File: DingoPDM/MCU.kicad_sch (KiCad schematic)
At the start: 23 parts, among them J4 TC, U3 PCA82C250, U4 STM32F303CCTx, Y1 8mHz

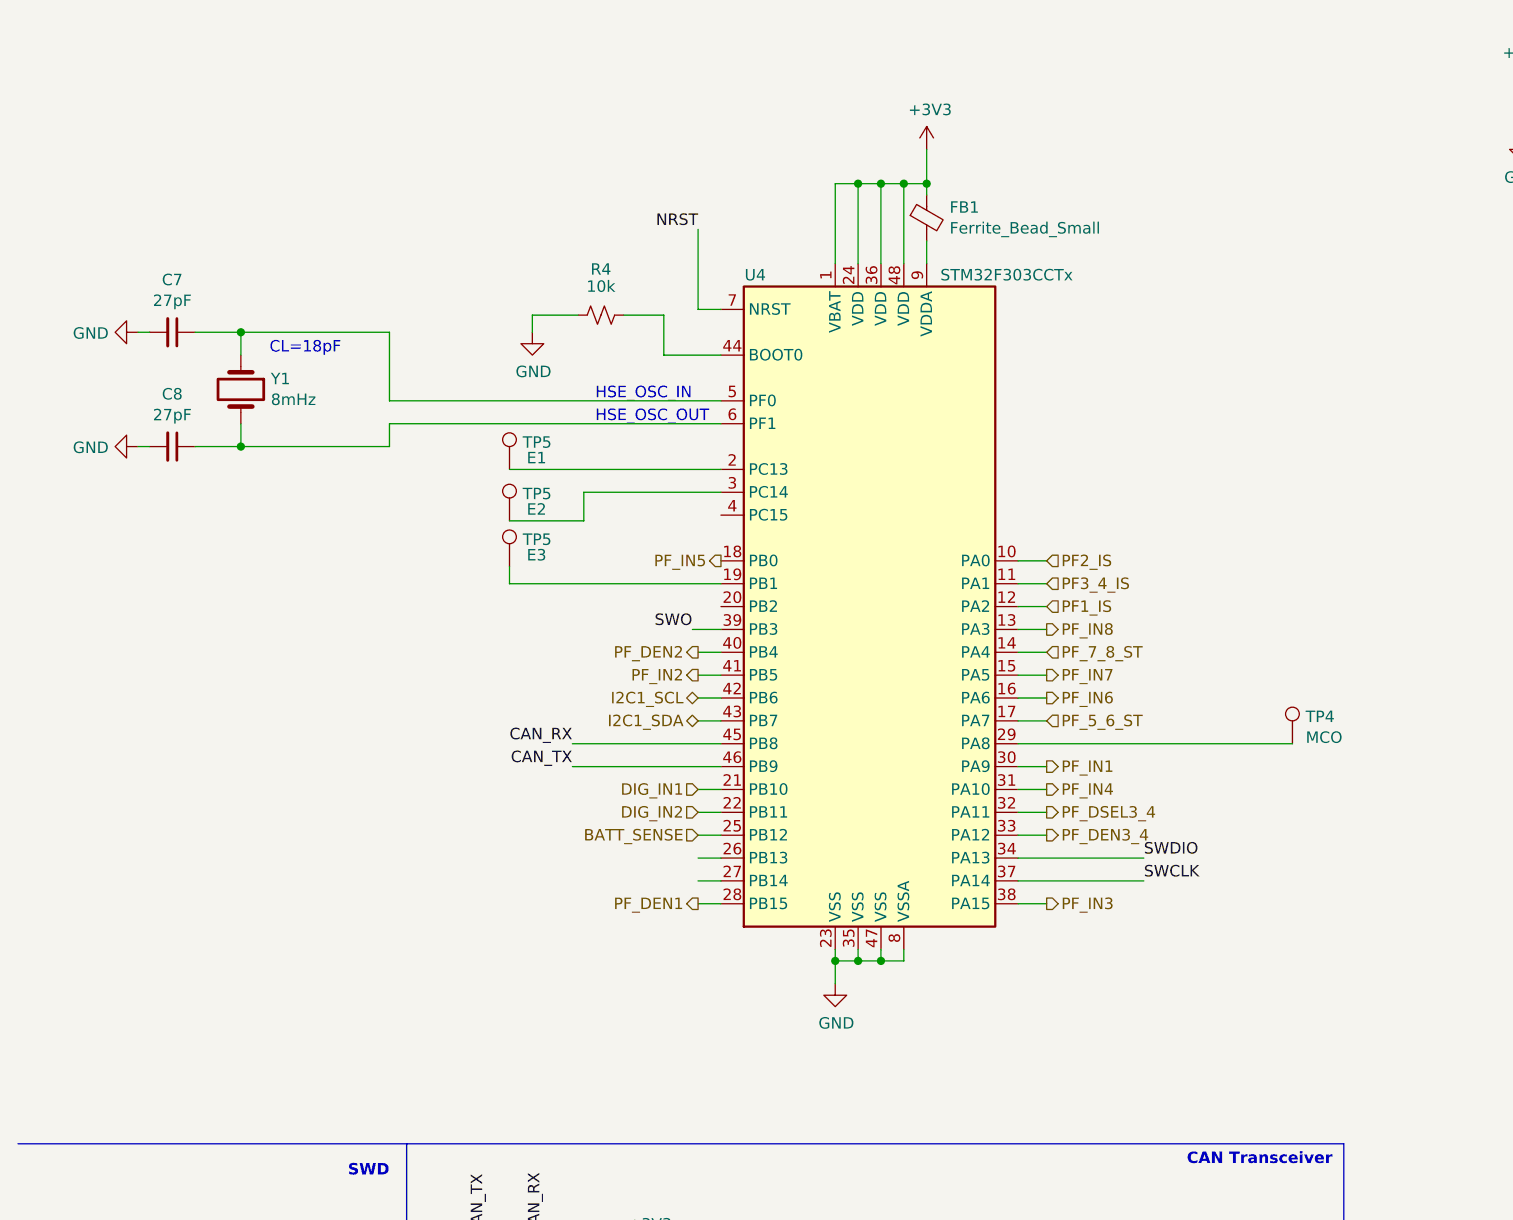
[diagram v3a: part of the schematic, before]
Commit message: Changed to STM32F446RE
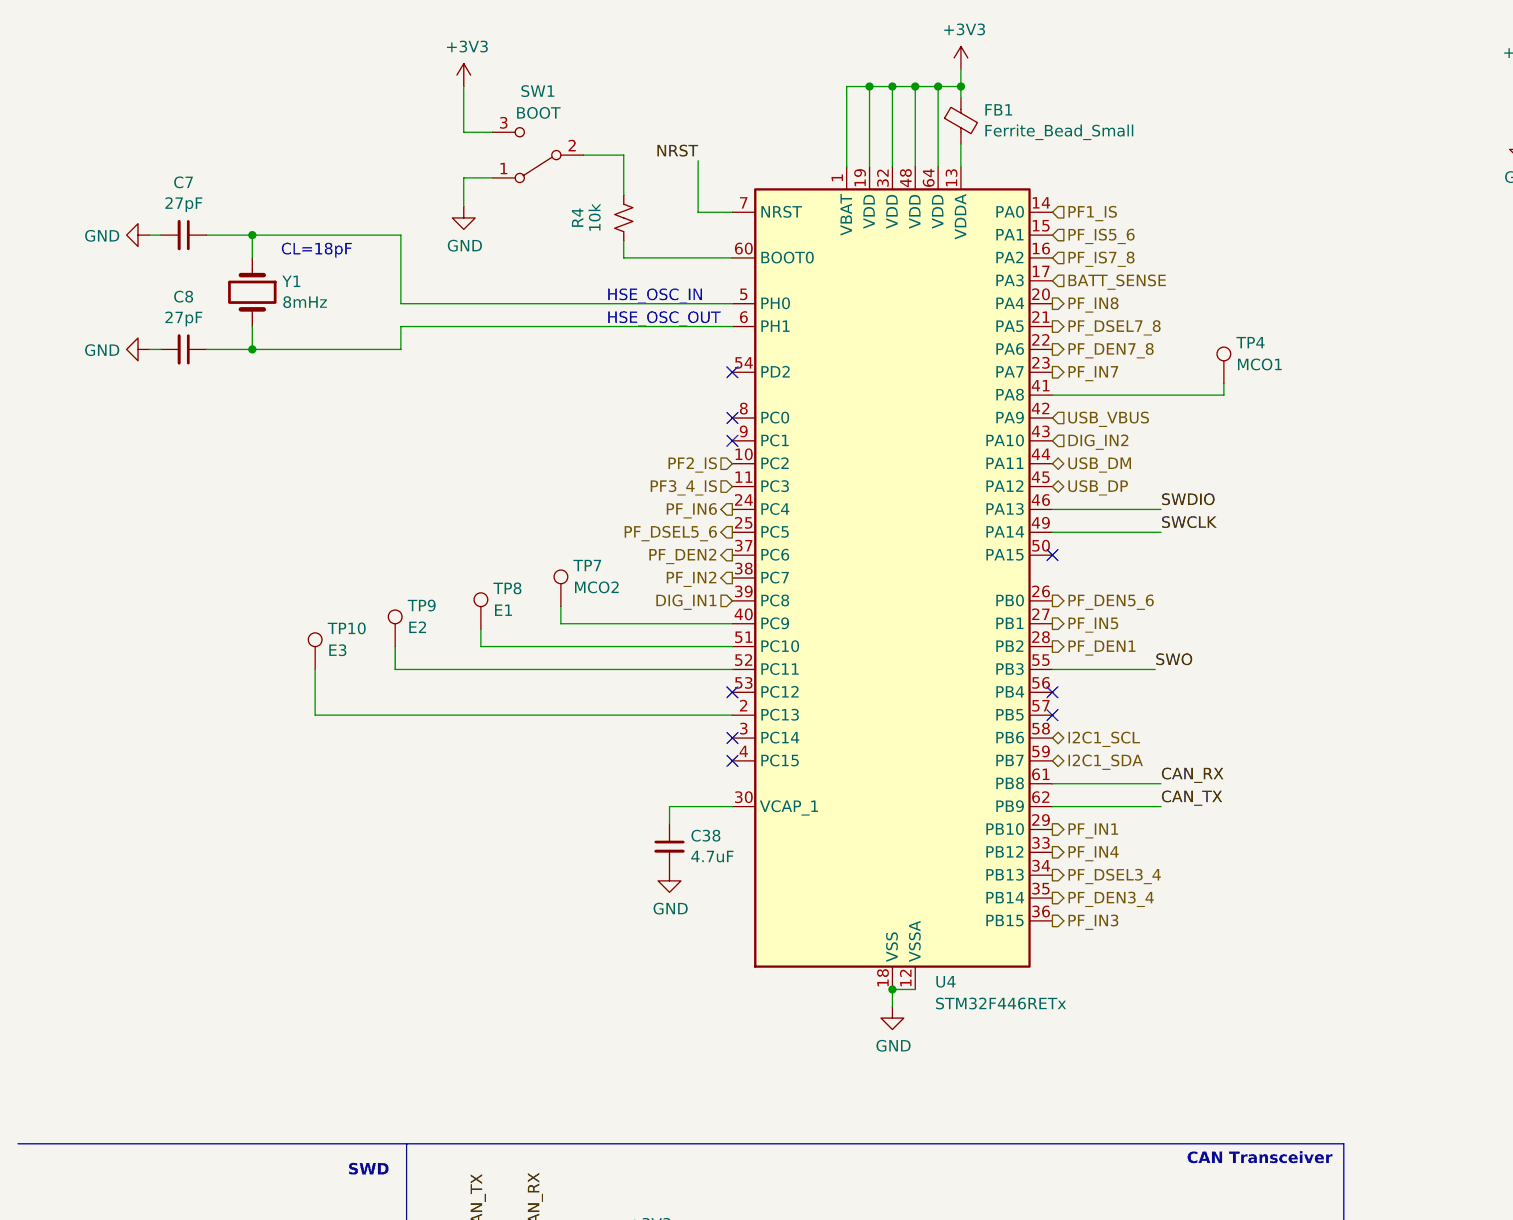
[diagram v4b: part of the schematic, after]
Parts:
- removed TP5: E1, TestPoint:TestPoint_Keystone_5000-5004_Miniature, symbol Connector:TestPoint
- removed TP5: E2, TestPoint:TestPoint_Keystone_5000-5004_Miniature, symbol Connector:TestPoint
- removed TP5: E3, TestPoint:TestPoint_Keystone_5000-5004_Miniature, symbol Connector:TestPoint
- removed U4: STM32F303CCTx, Package_QFP:LQFP-48_7x7mm_P0.5mm, symbol MCU_ST_STM32F3:STM32F303CCTx
- added C38: 4.7uF, Capacitor_SMD:C_0805_2012Metric, symbol Device:C_Small
- added SW1: BOOT, SlideSwitch:CJS-1200TB, symbol Switch:SW_SPDT
- added TP10: E3, TestPoint:TestPoint_Keystone_5000-5004_Miniature, symbol Connector:TestPoint
- added TP7: MCO2, TestPoint:TestPoint_Pad_D1.0mm, symbol Connector:TestPoint
- added TP8: E1, TestPoint:TestPoint_Keystone_5000-5004_Miniature, symbol Connector:TestPoint
- added TP9: E2, TestPoint:TestPoint_Keystone_5000-5004_Miniature, symbol Connector:TestPoint
- added U4: STM32F446RETx, Package_QFP:LQFP-64_10x10mm_P0.5mm, symbol MCU_ST_STM32F4:STM32F446RETx
- TP4: value MCO -> MCO1
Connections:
- net +3V3: now also SW1.3 (C), U4.1 (VBAT), U4.19 (VDD), U4.32 (VDD), U4.48 (VDD), U4.64 (VDD)
- net BATT_SENSE: now also U4.17 (PA3)
- net CAN_RX: now also U4.61 (PB8)
- net CAN_TX: now also U4.62 (PB9)
- net DIG_IN1: now also U4.39 (PC8)
- net DIG_IN2: now also U4.43 (PA10)
- net GND: now also C38.2, SW1.1 (A), U4.12 (VSSA), U4.18 (VSS), U4.31 (VSS), U4.47 (VSS), U4.63 (VSS); no longer R4.2
- net I2C1_SCL: now also U4.58 (PB6)
- net I2C1_SDA: now also U4.59 (PB7)
- net NRST: now also U4.7 (NRST)
- net PF1_IS: now also U4.14 (PA0)
- net PF2_IS: now also U4.10 (PC2)
- net PF3_4_IS: now also U4.11 (PC3)
- net PF_DEN1: now also U4.28 (PB2)
- net PF_DEN2: now also U4.37 (PC6)
- net PF_DEN3_4: now also U4.35 (PB14)
- net PF_DSEL3_4: now also U4.34 (PB13)
- net PF_IN1: now also U4.29 (PB10)
- net PF_IN2: now also U4.38 (PC7)
- net PF_IN3: now also U4.36 (PB15)
- net PF_IN4: now also U4.33 (PB12)
- net PF_IN5: now also U4.27 (PB1)
- net PF_IN6: now also U4.24 (PC4)
- net PF_IN7: now also U4.23 (PA7)
- net PF_IN8: now also U4.20 (PA4)
- net SWCLK: now also U4.49 (PA14)
- net SWDIO: now also U4.46 (PA13)
- net SWO: now also U4.55 (PB3)
- net at TP4.1: now also U4.41 (PA8)
- net at R4.1: now also SW1.2 (B)
- net at C7.1, Y1.1: now also U4.5 (PH0)
- net at C8.1, Y1.2: now also U4.6 (PH1)
- net at FB1.2: now also U4.13 (VDDA)
- new net: R4.2, U4.60 (BOOT0)
- new net: TP7.1, U4.40 (PC9)
- new net: TP8.1, U4.51 (PC10)
- new net: TP10.1, U4.2 (PC13)
- new net: TP9.1, U4.52 (PC11)
- new net: C38.1, U4.30 (VCAP_1)
- new net PF_DEN5_6: U4.26 (PB0)
- new net PF_DEN7_8: U4.22 (PA6)
- new net PF_DSEL5_6: U4.25 (PC5)
- new net PF_DSEL7_8: U4.21 (PA5)
- new net PF_IS5_6: U4.15 (PA1)
- new net PF_IS7_8: U4.16 (PA2)
- new net USB_DM: U4.44 (PA11)
- new net USB_DP: U4.45 (PA12)
- new net USB_VBUS: U4.42 (PA9)
- no-connect marks 0 -> 9
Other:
- moved on the sheet: C7, C8, FB1, R4, Y1

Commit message: Routed V7
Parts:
- removed TP4: MCO1, TestPoint:TestPoint_Pad_D1.0mm, symbol Connector:TestPoint
- removed TP7: MCO2, TestPoint:TestPoint_Pad_D1.0mm, symbol Connector:TestPoint
- added C39: 100nF, Capacitor_SMD:C_0805_2012Metric, symbol Device:C_Small
- C15: value 10nF -> 100nF; Digi-Key_PN 311-1136-1-ND -> 478-1395-1-ND; LCSC C1710 -> C49678
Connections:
- net +3V3: now also C39.1
- net DIG_IN1: now also U4.43 (PA10); no longer U4.39 (PC8)
- net DIG_IN2: now also U4.39 (PC8); no longer U4.43 (PA10)
- net GND: now also C39.2
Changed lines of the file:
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@@
   (junction (at 190.5 29.21) (diameter 0) (color 0 0 0 0)
   )
-  (junction (at 233.68 29.21) (diameter 0) (color 0 0 0 0)
-  )
   (junction (at 81.915 165.1) (diameter 0) (color 0 0 0 0)
   )
@@
   (junction (at 213.36 24.13) (diameter 0) (color 0 0 0 0)
   )
+  (junction (at 234.315 29.21) (diameter 0) (color 0 0 0 0)
+  )
+  (junction (at 234.315 24.13) (diameter 0) (color 0 0 0 0)
+  )
   (junction (at 201.93 29.21) (diameter 0) (color 0 0 0 0)
   )
@@
   (junction (at 111.76 23.495) (diameter 0) (color 0 0 0 0)
   )
-  (junction (at 233.68 24.13) (diameter 0) (color 0 0 0 0)
+  (junction (at 179.07 29.21) (diameter 0) (color 0 0 0 0)
+  )
+  (junction (at 179.07 24.13) (diameter 0) (color 0 0 0 0)
   )
   (junction (at 106.68 23.495) (diameter 0) (color 0 0 0 0)
@@
     (stroke (width 0) (type default))
   )
+  (wire (pts (xy 234.315 24.13) (xy 245.11 24.13))
+    (stroke (width 0) (type default))
+  )
+  (wire (pts (xy 234.315 29.21) (xy 245.11 29.21))
+    (stroke (width 0) (type default))
+  )
   (wire (pts (xy 111.125 167.64) (xy 130.175 167.64))
     (stroke (width 0) (type default))
@@
     (stroke (width 0) (type default))
   )
-  (wire (pts (xy 223.52 24.13) (xy 233.68 24.13))
-    (stroke (width 0) (type default))
-  )
   (wire (pts (xy 64.77 33.655) (xy 61.595 33.655))
     (stroke (width 0) (type default))
@@
     (stroke (width 0) (type default))
   )
-  (wire (pts (xy 233.68 29.21) (xy 245.11 29.21))
-    (stroke (width 0) (type default))
-  )
   (wire (pts (xy 54.61 50.165) (xy 54.61 52.705))
     (stroke (width 0) (type default))
@@
     (stroke (width 0) (type default))
   )
-  (wire (pts (xy 91.44 83.185) (xy 72.39 83.185))
-    (stroke (width 0) (type default))
-  )
   (wire (pts (xy 85.725 175.26) (xy 83.185 175.26))
     (stroke (width 0) (type default))
@@
     (stroke (width 0) (type default))
   )
-  (wire (pts (xy 127 57.785) (xy 146.05 57.785))
-    (stroke (width 0) (type default))
-  )
   (wire (pts (xy 79.375 165.1) (xy 81.915 165.1))
     (stroke (width 0) (type default))
@@
     (stroke (width 0) (type default))
   )
-  (wire (pts (xy 72.39 83.185) (xy 72.39 81.28))
-    (stroke (width 0) (type default))
-  )
   (wire (pts (xy 38.1 40.005) (xy 33.02 40.005))
     (stroke (width 0) (type default))
@@
     (stroke (width 0) (type default))
   )
-  (wire (pts (xy 233.68 24.13) (xy 245.11 24.13))
+  (wire (pts (xy 223.52 24.13) (xy 234.315 24.13))
     (stroke (width 0) (type default))
   )
@@
     (stroke (width 0) (type default))
   )
-  (wire (pts (xy 146.05 57.785) (xy 146.05 56.515))
-    (stroke (width 0) (type default))
-  )
   (wire (pts (xy 26.67 52.705) (xy 27.94 52.705))
     (stroke (width 0) (type default))
@@
     (stroke (width 0) (type default))
   )
-  (wire (pts (xy 223.52 29.21) (xy 233.68 29.21))
+  (wire (pts (xy 223.52 29.21) (xy 234.315 29.21))
     (stroke (width 0) (type default))
   )
@@
     (effects (font (size 1.27 1.27)) (justify right))
   )
-  (hierarchical_label "DIG_IN1" (shape input) (at 91.44 80.645 180) (fields_autoplaced)
+  (hierarchical_label "DIG_IN1" (shape input) (at 127 62.865 0) (fields_autoplaced)
+    (effects (font (size 1.27 1.27)) (justify left))
+  )
+  (hierarchical_label "CAN_L" (shape bidirectional) (at 140.335 172.72 0) (fields_autoplaced)
+    (effects (font (size 1.27 1.27)) (justify left))
+  )
+  (hierarchical_label "DIG_IN2" (shape input) (at 91.44 80.645 180) (fields_autoplaced)
     (effects (font (size 1.27 1.27)) (justify right))
-  )
-  (hierarchical_label "CAN_L" (shape bidirectional) (at 140.335 172.72 0) (fields_autoplaced)
-    (effects (font (size 1.27 1.27)) (justify left))
-  )
-  (hierarchical_label "DIG_IN2" (shape input) (at 127 62.865 0) (fields_autoplaced)
-    (effects (font (size 1.27 1.27)) (justify left))
   )
   (hierarchical_label "PF_DSEL3_4" (shape output) (at 127 111.125 0) (fields_autoplaced)
@@
         (path "/8948e307-9174-4227-9c28-3ff885e6e83d/00000000-0000-0000-0000-00005f4db108"
           (reference "C14") (unit 1)
-        )
-      )
-    )
-  )
-  (symbol (lib_id "Device:C_Small") (at 233.68 26.67 0) (unit 1)
-    (in_bom yes) (on_board yes) (dnp no)
-    (property "Reference" "C15" (at 236.0168 25.5016 0)
-      (effects (font (size 1.27 1.27)) (justify left))
-    )
-    (property "Value" "10nF" (at 236.0168 27.813 0)
-      (effects (font (size 1.27 1.27)) (justify left))
-    )
-    (property "Footprint" "Capacitor_SMD:C_0805_2012Metric" (at 233.68 26.67 0)
-      (effects (font (size 1.27 1.27)) hide)
-    )
-    (property "Datasheet" "" (at 233.68 26.67 0)
-      (effects (font (size 1.27 1.27)) hide)
-    )
-    (property "Digi-Key_PN" "311-1136-1-ND" (at 233.68 26.67 0)
-      (effects (font (size 1.27 1.27)) hide)
-    )
-    (property "LCSC" "C1710" (at 233.68 26.67 0)
-      (effects (font (size 1.27 1.27)) hide)
-    )
-    (pin "1")
-    (pin "2")
-    (instances
-      (project "DingoPDM"
-        (path "/8948e307-9174-4227-9c28-3ff885e6e83d/00000000-0000-0000-0000-00005f4db108"
-          (reference "C15") (unit 1)
         )
       )
@@
     )
   )
-  (symbol (lib_id "Connector:TestPoint") (at 72.39 81.28 0) (unit 1)
-    (in_bom yes) (on_board yes) (dnp no) (fields_autoplaced)
-    (property "Reference" "TP7" (at 73.787 76.7659 0)
-      (effects (font (size 1.27 1.27)) (justify left))
-    )
-    (property "Value" "MCO2" (at 73.787 79.1901 0)
-      (effects (font (size 1.27 1.27)) (justify left))
-    )
-    (property "Footprint" "TestPoint:TestPoint_Pad_D1.0mm" (at 77.47 81.28 0)
-      (effects (font (size 1.27 1.27)) hide)
-    )
-    (property "Datasheet" "~" (at 77.47 81.28 0)
-      (effects (font (size 1.27 1.27)) hide)
-    )
-    (pin "1")
-    (instances
-      (project "DingoPDM"
-        (path "/8948e307-9174-4227-9c28-3ff885e6e83d/00000000-0000-0000-0000-00005f4db108"
-          (reference "TP7") (unit 1)
+  (symbol (lib_id "Device:C_Small") (at 179.07 26.67 0) (unit 1)
+    (in_bom yes) (on_board yes) (dnp no)
+    (property "Reference" "C39" (at 181.4068 25.5016 0)
+      (effects (font (size 1.27 1.27)) (justify left))
+    )
+    (property "Value" "100nF" (at 181.4068 27.813 0)
+      (effects (font (size 1.27 1.27)) (justify left))
+    )
+    (property "Footprint" "Capacitor_SMD:C_0805_2012Metric" (at 179.07 26.67 0)
+      (effects (font (size 1.27 1.27)) hide)
+    )
+    (property "Datasheet" "" (at 179.07 26.67 0)
+      (effects (font (size 1.27 1.27)) hide)
+    )
+    (property "Digi-Key_PN" "478-1395-1-ND" (at 179.07 26.67 0)
+      (effects (font (size 1.27 1.27)) hide)
+    )
+    (property "LCSC" "C49678" (at 179.07 26.67 0)
+      (effects (font (size 1.27 1.27)) hide)
+    )
+    (pin "1")
+    (pin "2")
+    (instances
+      (project "DingoPDM"
+        (path "/8948e307-9174-4227-9c28-3ff885e6e83d/00000000-0000-0000-0000-00005f4db108"
+          (reference "C39") (unit 1)
         )
       )
@@
         (path "/8948e307-9174-4227-9c28-3ff885e6e83d/00000000-0000-0000-0000-00005f4db108"
           (reference "C38") (unit 1)
-        )
-      )
-    )
-  )
-  (symbol (lib_id "Connector:TestPoint") (at 146.05 56.515 0) (unit 1)
-    (in_bom yes) (on_board yes) (dnp no) (fields_autoplaced)
-    (property "Reference" "TP4" (at 147.447 52.0009 0)
-      (effects (font (size 1.27 1.27)) (justify left))
-    )
-    (property "Value" "MCO1" (at 147.447 54.4251 0)
-      (effects (font (size 1.27 1.27)) (justify left))
-    )
-    (property "Footprint" "TestPoint:TestPoint_Pad_D1.0mm" (at 151.13 56.515 0)
-      (effects (font (size 1.27 1.27)) hide)
-    )
-    (property "Datasheet" "~" (at 151.13 56.515 0)
-      (effects (font (size 1.27 1.27)) hide)
-    )
-    (pin "1")
-    (instances
-      (project "DingoPDM"
-        (path "/8948e307-9174-4227-9c28-3ff885e6e83d/00000000-0000-0000-0000-00005f4db108"
-          (reference "TP4") (unit 1)
         )
       )
@@
         )
       )
+    )
+  )
+  (symbol (lib_id "Device:C_Small") (at 234.315 26.67 0) (unit 1)
+    (in_bom yes) (on_board yes) (dnp no)
+    (property "Reference" "C15" (at 236.6518 25.5016 0)
+      (effects (font (size 1.27 1.27)) (justify left))
+    )
+    (property "Value" "100nF" (at 236.6518 27.813 0)
+      (effects (font (size 1.27 1.27)) (justify left))
+    )
+    (property "Footprint" "Capacitor_SMD:C_0805_2012Metric" (at 234.315 26.67 0)
+      (effects (font (size 1.27 1.27)) hide)
+    )
+    (property "Datasheet" "" (at 234.315 26.67 0)
+      (effects (font (size 1.27 1.27)) hide)
+    )
+    (property "Digi-Key_PN" "478-1395-1-ND" (at 234.315 26.67 0)
+      (effects (font (size 1.27 1.27)) hide)
+    )
+    (property "LCSC" "C49678" (at 234.315 26.67 0)
+      (effects (font (size 1.27 1.27)) hide)
+    )
+    (pin "1")
+    (pin "2")
+    (instances
+      (project "DingoPDM"
+        (path "/8948e307-9174-4227-9c28-3ff885e6e83d/00000000-0000-0000-0000-00005f4db108"
+          (reference "C15") (unit 1)
+        )
+      )

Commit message: Small edits
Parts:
- R4: value 10k -> 10K
- R5: value 1k -> 1K
- SW1: Digi-Key_PN 563-1022-1-ND -> 563-CJS-1200TB1CT-ND; LCSC (none) -> C2921631
- U4: Digi-Key_PN (none) -> 497-15376-ND; LCSC (none) -> C69336
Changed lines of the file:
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@@
       (effects (font (size 1.27 1.27)))
     )
-    (property "Value" "10k" (at 76.2 38.1 90)
+    (property "Value" "10K" (at 76.2 38.1 90)
       (effects (font (size 1.27 1.27)))
     )
@@
       (effects (font (size 1.27 1.27)) (justify right))
     )
-    (property "Value" "1k" (at 76.835 160.02 0)
+    (property "Value" "1K" (at 76.835 160.02 0)
       (effects (font (size 1.27 1.27)) (justify right))
     )
@@
       (effects (font (size 1.27 1.27)) hide)
     )
-    (property "Digi-Key_PN" "563-1022-1-ND" (at 69.85 31.115 0)
+    (property "Digi-Key_PN" "563-CJS-1200TB1CT-ND" (at 69.85 31.115 0)
+      (effects (font (size 1.27 1.27)) hide)
+    )
+    (property "LCSC" "C2921631" (at 69.85 31.115 0)
       (effects (font (size 1.27 1.27)) hide)
     )
@@
       (effects (font (size 1.27 1.27)) hide)
     )
+    (property "Digi-Key_PN" "497-15376-ND" (at 109.22 78.105 0)
+      (effects (font (size 1.27 1.27)) hide)
+    )
+    (property "LCSC" "C69336" (at 109.22 78.105 0)
+      (effects (font (size 1.27 1.27)) hide)
+    )
